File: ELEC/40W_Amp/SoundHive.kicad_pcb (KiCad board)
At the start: 2 copper layers, 42.7 x 46.7 mm, 187 parts, among them J1 CONN_01X08, J2 CONN_01X08, J3 Screw_Terminal_1x02, J4 CONN_01X02_MALE, J5 CONN_01X02_MALE, J6 CONN_01X02_MALE, J7 CONN_01X03_MALE, J8 CONN_01X01, U1 TPA3106D1

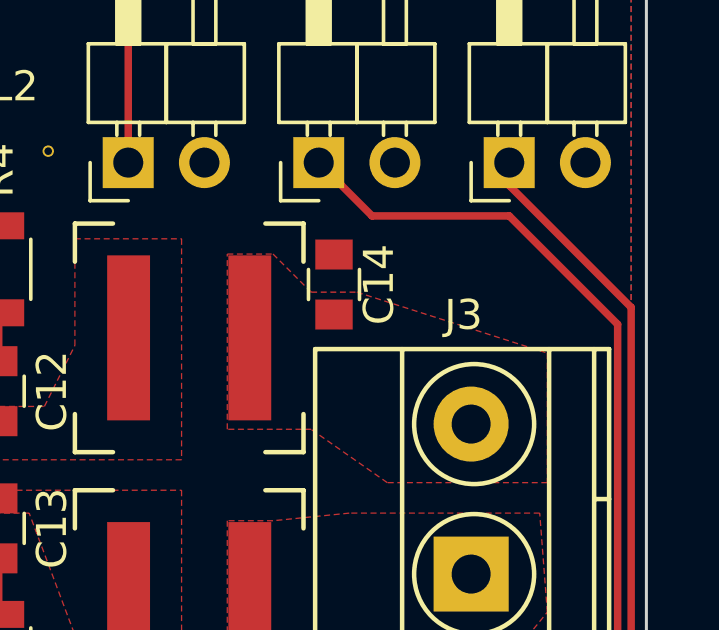
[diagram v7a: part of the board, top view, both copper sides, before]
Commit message: Traded connector for something that actually fits
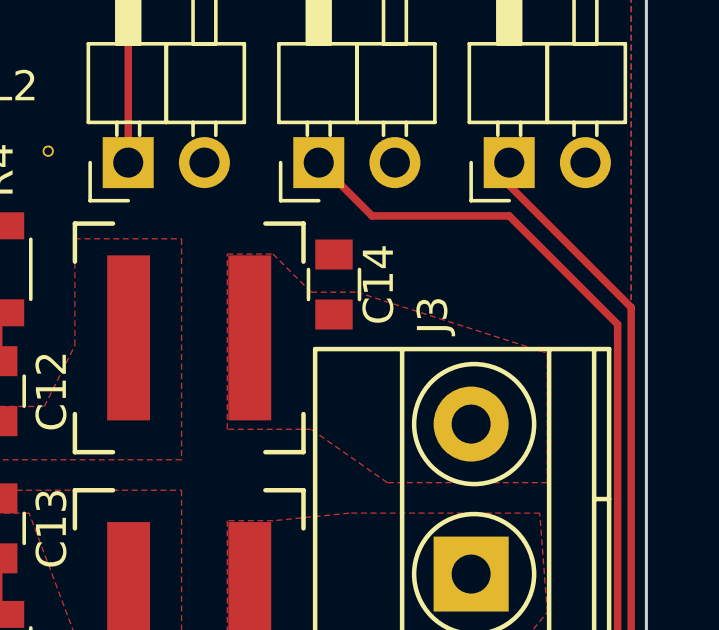
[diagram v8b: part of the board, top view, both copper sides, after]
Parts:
- J3: footprint Connectors_Terminal_Blocks.pretty:TerminalBlock_Pheonix_MKDS1.5-2pol -> Connectors_Terminal_Blocks.pretty:TerminalBlock_OSTTC022162
- R4, R5: value 20R 1/4 W, 5% -> 20R 1/4 W - 1%
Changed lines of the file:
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@@
     (links 236)
     (no_connects 2)
-    (area 94.641999 75.230666 138.727 127.461333)
+    (area 94.691999 77.927999 137.464001 124.764001)
     (thickness 1.6)
     (drawings 14)
@@
       (effects (font (size 1 1) (thickness 0.15)))
     )
-    (fp_text value "20R 1/4 W, 5%" (at 0 1.95 270) (layer F.Fab)
+    (fp_text value "20R 1/4 W - 1%" (at 0 1.95 270) (layer F.Fab)
       (effects (font (size 1 1) (thickness 0.15)))
     )
@@
       (effects (font (size 1 1) (thickness 0.15)))
     )
-    (fp_text value "20R 1/4 W, 5%" (at 0 1.95 270) (layer F.Fab)
+    (fp_text value "20R 1/4 W - 1%" (at 0 1.95 270) (layer F.Fab)
       (effects (font (size 1 1) (thickness 0.15)))
     )
@@
     )
   )
-  (module Connectors_Terminal_Blocks.pretty:TerminalBlock_Pheonix_MKDS1.5-2pol (layer F.Cu)
-    (at 131.572 104.14 90)
-    (descr "2-way 5mm pitch terminal block, Phoenix MKDS series")
-    (fp_text reference J3 (at 8.636 -0.254 180) (layer F.SilkS)
-      (effects (font (size 1 1) (thickness 0.15)))
-    )
-    (fp_text value Screw_Terminal_1x02 (at 2.5 -6.6 90) (layer F.Fab)
-      (effects (font (size 1 1) (thickness 0.15)))
-    )
-    (fp_line (start -2.7 -5.4) (end 7.7 -5.4) (layer F.CrtYd) (width 0.05))
-    (fp_line (start -2.7 4.8) (end -2.7 -5.4) (layer F.CrtYd) (width 0.05))
-    (fp_line (start 7.7 4.8) (end -2.7 4.8) (layer F.CrtYd) (width 0.05))
-    (fp_line (start 7.7 -5.4) (end 7.7 4.8) (layer F.CrtYd) (width 0.05))
-    (fp_line (start 2.5 4.1) (end 2.5 4.6) (layer F.SilkS) (width 0.15))
-    (fp_circle (center 5 0.1) (end 3 0.1) (layer F.SilkS) (width 0.15))
-    (fp_circle (center 0 0.1) (end 2 0.1) (layer F.SilkS) (width 0.15))
-    (fp_line (start -2.5 2.6) (end 7.5 2.6) (layer F.SilkS) (width 0.15))
-    (fp_line (start -2.5 -2.3) (end 7.5 -2.3) (layer F.SilkS) (width 0.15))
-    (fp_line (start -2.5 4.1) (end 7.5 4.1) (layer F.SilkS) (width 0.15))
-    (fp_line (start -2.5 4.6) (end 7.5 4.6) (layer F.SilkS) (width 0.15))
-    (fp_line (start 7.5 4.6) (end 7.5 -5.2) (layer F.SilkS) (width 0.15))
-    (fp_line (start 7.5 -5.2) (end -2.5 -5.2) (layer F.SilkS) (width 0.15))
-    (fp_line (start -2.5 -5.2) (end -2.5 4.6) (layer F.SilkS) (width 0.15))
-    (pad 1 thru_hole rect (at 0 0 90) (size 2.5 2.5) (drill 1.3) (layers *.Cu *.Mask)
-      (net 19 "Net-(C15-Pad1)"))
-    (pad 2 thru_hole circle (at 5 0 90) (size 2.5 2.5) (drill 1.3) (layers *.Cu *.Mask)
-      (net 18 "Net-(C14-Pad2)"))
-    (model ${KIPRJMOD}/../Libraries/3d_models/TerminalBlock_Pheonix_MKDS1.5-2pol.wrl
-      (at (xyz 0.0984 0 0))
-      (scale (xyz 1 1 1))
-      (rotate (xyz 0 0 0))
-    )
-  )
   (module Capacitors_SMD:C_0805 (layer F.Cu)
     (at 115.824 102.616 90)
@@
       (net 28 "Net-(J8-Pad1)"))
   )
+  (module Connectors_Terminal_Blocks.pretty:TerminalBlock_OSTTC022162 (layer F.Cu)
+    (at 131.572 104.14 90)
+    (descr "2-way 5mm pitch terminal block")
+    (fp_text reference J3 (at 8.636 -1.27 90) (layer F.SilkS)
+      (effects (font (size 1 1) (thickness 0.15)))
+    )
+    (fp_text value Screw_Terminal_1x02 (at 2.5 -6.6 90) (layer F.Fab)
+      (effects (font (size 1 1) (thickness 0.15)))
+    )
+    (fp_line (start -2.7 -5.4) (end 7.7 -5.4) (layer F.CrtYd) (width 0.05))
+    (fp_line (start -2.7 4.8) (end -2.7 -5.4) (layer F.CrtYd) (width 0.05))
+    (fp_line (start 7.7 4.8) (end -2.7 4.8) (layer F.CrtYd) (width 0.05))
+    (fp_line (start 7.7 -5.4) (end 7.7 4.8) (layer F.CrtYd) (width 0.05))
+    (fp_line (start 2.5 4.1) (end 2.5 4.6) (layer F.SilkS) (width 0.15))
+    (fp_circle (center 5 0.1) (end 3 0.1) (layer F.SilkS) (width 0.15))
+    (fp_circle (center 0 0.1) (end 2 0.1) (layer F.SilkS) (width 0.15))
+    (fp_line (start -2.5 2.6) (end 7.5 2.6) (layer F.SilkS) (width 0.15))
+    (fp_line (start -2.5 -2.3) (end 7.5 -2.3) (layer F.SilkS) (width 0.15))
+    (fp_line (start -2.5 4.1) (end 7.5 4.1) (layer F.SilkS) (width 0.15))
+    (fp_line (start -2.5 4.6) (end 7.5 4.6) (layer F.SilkS) (width 0.15))
+    (fp_line (start 7.5 4.6) (end 7.5 -5.2) (layer F.SilkS) (width 0.15))
+    (fp_line (start 7.5 -5.2) (end -2.5 -5.2) (layer F.SilkS) (width 0.15))
+    (fp_line (start -2.5 -5.2) (end -2.5 4.6) (layer F.SilkS) (width 0.15))
+    (pad 1 thru_hole rect (at 0 0 90) (size 2.5 2.5) (drill 1.3) (layers *.Cu *.Mask)
+      (net 19 "Net-(C15-Pad1)"))
+    (pad 2 thru_hole circle (at 5 0 90) (size 2.5 2.5) (drill 1.3) (layers *.Cu *.Mask)
+      (net 18 "Net-(C14-Pad2)"))
+    (model ${KIPRJMOD}/../Libraries/3d_models/OSTTC022162.wrl
+      (at (xyz 0.1 0 0))
+      (scale (xyz 400 400 400))
+      (rotate (xyz 0 0 0))
+    )
+  )
   (gr_line (start 137.414 77.978) (end 94.742 77.978) (angle 90) (layer Edge.Cuts) (width 0.1))
